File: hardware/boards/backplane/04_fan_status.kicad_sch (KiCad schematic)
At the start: 14 parts, among them J11 12V 3-WIRE FAN, J12 DS18B20 EXT SUPPLY, J9 12V 3-WIRE FAN, Q1 AO3407A, Q2 2N7002, Q3 AO3407A, Q4 2N7002

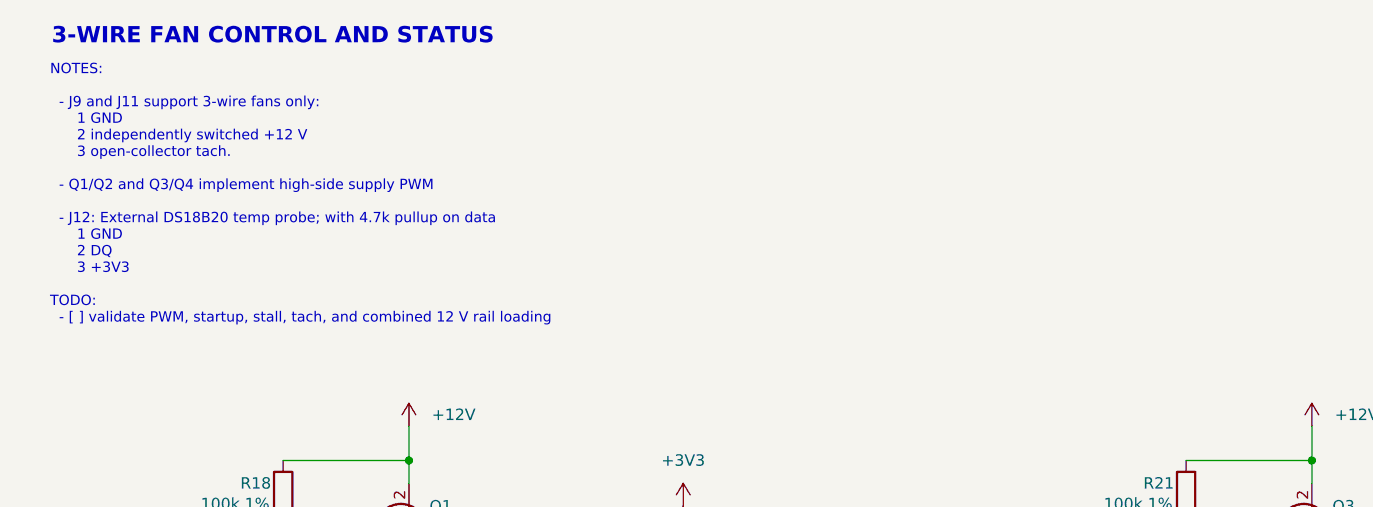
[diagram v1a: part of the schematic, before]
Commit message: Refine prototype Kelvin pours and input grounding; add test TODOs
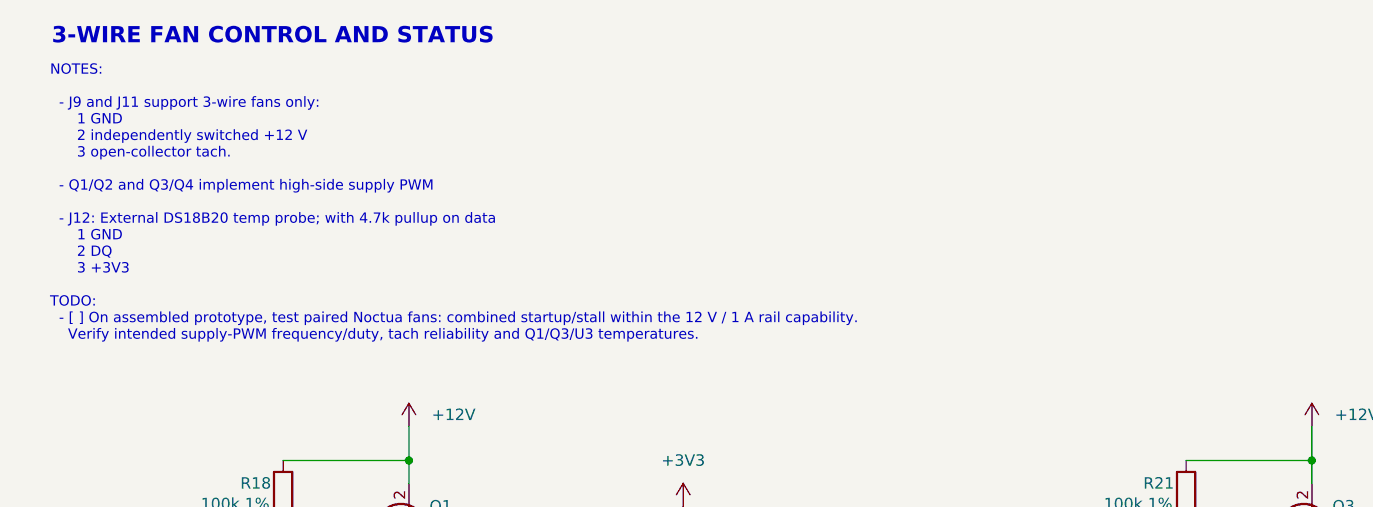
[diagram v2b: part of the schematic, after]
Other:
- note added: "NOTES: - J9 and J11 support 3-wire fans only: 1 GND 2 independently switched +12 V 3 open-collector tach. - Q1/Q2 and Q3/Q4 implement high-side supply PWM - J12: External DS18B20 temp probe; with 4.7k pullup on data 1 GND 2 DQ 3 +3V3 TODO: - [ ] On assembled prototype, test paired Noctua fans: combined startup/stall within the 12 V / 1 A rail capability. Verify intended supply-PWM frequency/duty,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"
- note removed: "NOTES: - J9 and J11 support 3-wire fans only: 1 GND 2 independently switched +12 V 3 open-collector tach. - Q1/Q2 and Q3/Q4 implement high-side supply PWM - J12: External DS18B20 temp probe; with 4.7k pullup on data 1 GND 2 DQ 3 +3V3 TODO: - [ ] validate PWM, startup, stall, tach, and combined 12 V rail loading"
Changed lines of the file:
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@@
 	(generator_version "10.0")
 	(paper "A4")
-	(text "NOTES:\n\n  - J9 and J11 support 3-wire fans only: \n      1 GND\n      2 independently switched +12 V\n      3 open-collector tach. \n\n  - Q1/Q2 and Q3/Q4 implement high-side supply PWM\n\n  - J12: External DS18B20 temp probe; with 4.7k pullup on data\n      1 GND\n      2 DQ\n      3 +3V3\n\nTODO:\n  - [ ] validate PWM, startup, stall, tach, and combined 12 V rail loading\n\n"
+	(text "NOTES:\n\n  - J9 and J11 support 3-wire fans only: \n      1 GND\n      2 independently switched +12 V\n      3 open-collector tach. \n\n  - Q1/Q2 and Q3/Q4 implement high-side supply PWM\n\n  - J12: External DS18B20 temp probe; with 4.7k pullup on data\n      1 GND\n      2 DQ\n      3 +3V3\n\nTODO:\n  - [ ] On assembled prototype, test paired Noctua fans: combined startup/stall within the 12 V / 1 A rail capability.\n    Verify intended supply-PWM frequency/duty, tach reliability and Q1/Q3/U3 temperatures.\n\n"
 		(exclude_from_sim no)
-		(at 19.812 50.292 0)
+		(at 19.812 52.197 0)
 		(effects
 			(font
